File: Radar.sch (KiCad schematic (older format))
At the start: 9 parts

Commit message: fixed library
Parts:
- U? (x3): symbol own:PA -> Radar-rescue:PA-own
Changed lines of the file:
@@
 	7350 3400 7200 3400
 $Comp
-L own:PA U?
+L Radar-rescue:PA-own U?
 U 1 1 5F894269
 P 7800 5200
@@
 $EndComp
 $Comp
-L own:PA U?
+L Radar-rescue:PA-own U?
 U 1 1 5F895397
 P 6700 5200
@@
 $EndComp
 $Comp
-L own:PA U?
+L Radar-rescue:PA-own U?
 U 1 1 5F8A3F2E
 P 5650 5200

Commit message: Architecture of IF
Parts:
- removed U?: PA, symbol Radar-rescue:PA-own
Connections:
- wire segments 8 -> 7
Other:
- moved on the sheet: J?
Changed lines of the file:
@@
 F4 "VCO_TUNE_IN" I L 4950 2500 50
 $EndSheet
-$Sheet
-S 2300 2000 2200 3600
-U 5F88615A
-F0 "Digital" 50
-F1 "digital.sch" 50
-F2 "IF_IN_P" I R 4500 5100 50
-F3 "VCO_TUNE_OUT" O R 4500 2500 50
-F4 "IF_IN_N" I R 4500 5300 50
-$EndSheet
 Wire Wire Line
-	4950 5100 4500 5100
+	4950 5200 4500 5200
 Wire Wire Line
 	4500 2500 4950 2500
 Wire Wire Line
-	8650 2500 7700 2500
+	8200 2500 7700 2500
 Wire Notes Line style solid rgb(132, 0, 0)
 	5500 2500 5650 2500
@@
 L Radar-rescue:PA-own U?
 U 1 1 5F894269
-P 7800 5200
-F 0 "U?" H 7800 5550 50  0001 C CNN
-F 1 "LNA" H 7800 5200 50  0000 R CNN
-F 2 "" H 7800 5200 50  0001 C CNN
-F 3 "" H 7800 5200 50  0001 C CNN
-	1    7800 5200
+P 7400 5200
+F 0 "U?" H 7400 5550 50  0001 C CNN
+F 1 "LNA" H 7400 5200 50  0000 R CNN
+F 2 "" H 7400 5200 50  0001 C CNN
+F 3 "" H 7400 5200 50  0001 C CNN
+	1    7400 5200
 	-1   0    0    1
 $EndComp
@@
 L Radar-rescue:PA-own U?
 U 1 1 5F895397
-P 6700 5200
-F 0 "U?" H 6700 5550 50  0001 C CNN
-F 1 "PA" H 6750 5450 50  0001 R CNN
-F 2 "" H 6700 5200 50  0001 C CNN
-F 3 "" H 6700 5200 50  0001 C CNN
-	1    6700 5200
+P 6300 5200
+F 0 "U?" H 6300 5550 50  0001 C CNN
+F 1 "PA" H 6350 5450 50  0001 R CNN
+F 2 "" H 6300 5200 50  0001 C CNN
+F 3 "" H 6300 5200 50  0001 C CNN
+	1    6300 5200
 	-1   0    0    1
 $EndComp
 Wire Notes Line style solid rgb(132, 0, 0)
-	7250 4200 8050 4200
+	6850 4200 7650 4200
 Wire Notes Line style solid rgb(132, 0, 0)
-	7050 5200 6900 5200
+	6650 5200 6500 5200
 Wire Notes Line style solid rgb(132, 0, 0)
-	8000 5200 8050 5200
+	7600 5200 7650 5200
 Wire Notes Line style solid rgb(132, 0, 0)
-	7250 4200 7250 5000
+	6850 4200 6850 5000
 Wire Notes Line style solid rgb(132, 0, 0)
-	7600 5200 7450 5200
+	7200 5200 7050 5200
 $Sheet
-S 4950 4000 3400 1600
+S 4950 4000 3000 1600
 U 5F88609A
 F0 "Receiver" 50
 F1 "receiver.sch" 50
-F2 "LO_IN" I R 8350 4200 50
-F3 "RF_IN" I R 8350 5200 50
-F4 "IF_OUT_P" O L 4950 5100 50
-F5 "IF_OUT_N" O L 4950 5300 50
+F2 "LO_IN" I R 7950 4200 50
+F3 "RF_IN" I R 7950 5200 50
+F4 "IF_OUT" O L 4950 5200 50
 $EndSheet
 $Comp
 L own:mixer_diagram U?
 U 1 1 5F890667
-P 7250 5200
-F 0 "U?" H 7250 4850 50  0001 C CNN
-F 1 "mixer_diagram" H 7250 5500 50  0001 C CNN
-F 2 "" H 7250 5200 50  0001 C CNN
-F 3 "" H 7250 5200 50  0001 C CNN
-	1    7250 5200
+P 6850 5200
+F 0 "U?" H 6850 4850 50  0001 C CNN
+F 1 "mixer_diagram" H 6850 5500 50  0001 C CNN
+F 2 "" H 6850 5200 50  0001 C CNN
+F 3 "" H 6850 5200 50  0001 C CNN
+	1    6850 5200
 	1    0    0    -1
 $EndComp
@@
 L own:lowpass_diagram U?
 U 1 1 5F89837D
-P 6200 5200
-F 0 "U?" H 6200 5450 50  0001 C CNN
-F 1 "lowpass_diagram" H 6200 4950 50  0001 C CNN
-F 2 "" H 6200 5200 50  0001 C CNN
-F 3 "" H 6200 5200 50  0001 C CNN
-	1    6200 5200
+P 5800 5200
+F 0 "U?" H 5800 5450 50  0001 C CNN
+F 1 "lowpass_diagram" H 5800 4950 50  0001 C CNN
+F 2 "" H 5800 5200 50  0001 C CNN
+F 3 "" H 5800 5200 50  0001 C CNN
+	1    5800 5200
 	1    0    0    -1
 $EndComp
@@
 	6550 2500 7350 2500
 Wire Notes Line style solid rgb(132, 0, 0)
-	6500 5200 6400 5200
-Wire Notes Line style solid rgb(132, 0, 0)
-	6000 5200 5850 5200
+	6100 5200 6000 5200
 $Comp
 L Connector:Conn_Coaxial J?
 U 1 1 5F89AF4D
-P 8850 2500
-F 0 "J?" H 8950 2475 50  0000 L CNN
-F 1 "Transmit Antenna" H 8450 2650 50  0000 L CNN
-F 2 "" H 8850 2500 50  0001 C CNN
-F 3 " ~" H 8850 2500 50  0001 C CNN
-	1    8850 2500
+P 8400 2500
+F 0 "J?" H 8500 2475 50  0000 L CNN
+F 1 "Transmit Antenna" H 8000 2650 50  0000 L CNN
+F 2 "" H 8400 2500 50  0001 C CNN
+F 3 " ~" H 8400 2500 50  0001 C CNN
+	1    8400 2500
 	1    0    0    -1
 $EndComp
@@
 L Connector:Conn_Coaxial J?
 U 1 1 5F89BD12
-P 8800 5200
-F 0 "J?" H 8900 5175 50  0000 L CNN
-F 1 "Receive Antenna" H 8500 5350 50  0000 L CNN
-F 2 "" H 8800 5200 50  0001 C CNN
-F 3 " ~" H 8800 5200 50  0001 C CNN
-	1    8800 5200
+P 8400 5200
+F 0 "J?" H 8500 5175 50  0000 L CNN
+F 1 "Receive Antenna" H 8100 5350 50  0000 L CNN
+F 2 "" H 8400 5200 50  0001 C CNN
+F 3 " ~" H 8400 5200 50  0001 C CNN
+	1    8400 5200
 	1    0    0    -1
 $EndComp
@@
 L power:GND #PWR?
 U 1 1 5F89C296
-P 8850 2700
-F 0 "#PWR?" H 8850 2450 50  0001 C CNN
-F 1 "GND" H 8855 2527 50  0000 C CNN
-F 2 "" H 8850 2700 50  0001 C CNN
-F 3 "" H 8850 2700 50  0001 C CNN
-	1    8850 2700
+P 8400 2700
+F 0 "#PWR?" H 8400 2450 50  0001 C CNN
+F 1 "GND" H 8405 2527 50  0000 C CNN
+F 2 "" H 8400 2700 50  0001 C CNN
+F 3 "" H 8400 2700 50  0001 C CNN
+	1    8400 2700
 	1    0    0    -1
 $EndComp
@@
 L power:GND #PWR?
 U 1 1 5F89C6F1
-P 8800 5400
-F 0 "#PWR?" H 8800 5150 50  0001 C CNN
-F 1 "GND" H 8805 5227 50  0000 C CNN
-F 2 "" H 8800 5400 50  0001 C CNN
-F 3 "" H 8800 5400 50  0001 C CNN
-	1    8800 5400
+P 8400 5400
+F 0 "#PWR?" H 8400 5150 50  0001 C CNN
+F 1 "GND" H 8405 5227 50  0000 C CNN
+F 2 "" H 8400 5400 50  0001 C CNN
+F 3 "" H 8400 5400 50  0001 C CNN
+	1    8400 5400
 	1    0    0    -1
 $EndComp
-$Comp
-L Radar-rescue:PA-own U?
-U 1 1 5F8A3F2E
-P 5650 5200
-F 0 "U?" H 5650 5550 50  0001 C CNN
-F 1 "PA" H 5700 5450 50  0001 R CNN
-F 2 "" H 5650 5200 50  0001 C CNN
-F 3 "" H 5650 5200 50  0001 C CNN
-	1    5650 5200
-	-1   0    0    1
-$EndComp
 Wire Wire Line
-	8350 5200 8600 5200
+	7950 5200 8200 5200
 Wire Wire Line
-	4950 5300 4500 5300
+	8100 3400 8100 4200
 Wire Wire Line
-	8500 3400 8500 4200
+	8100 4200 7950 4200
 Wire Wire Line
-	8500 4200 8350 4200
-Wire Wire Line
-	7700 3400 8500 3400
-Wire Notes Line style solid rgb(132, 0, 0)
-	5650 5100 5350 5100
-Wire Notes Line style solid rgb(132, 0, 0)
-	5650 5300 5350 5300
+	7700 3400 8100 3400
 Wire Notes Line
 	4800 1800 4800 5850
@@
 Text Notes 4550 1950 2    100  ~ 0
 Digital Board
+$Sheet
+S 2300 2000 2200 3600
+U 5F88615A
+F0 "Digital" 50
+F1 "digital.sch" 50
+F2 "IF_IN" I R 4500 5200 50
+F3 "VCO_TUNE_OUT" O R 4500 2500 50
+$EndSheet
+Wire Notes Line style solid rgb(132, 0, 0)
+	5350 5200 5600 5200
 $EndSCHEMATC

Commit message: Finished IF
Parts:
- removed J?: Receive Antenna, symbol Connector:Conn_Coaxial
- removed U?: mixer_diagram, symbol own:mixer_diagram
- removed U?: LNA, symbol Radar-rescue:PA-own
- removed U?: PA, symbol Radar-rescue:PA-own
- removed U?: lowpass_diagram, symbol own:lowpass_diagram
- added J1: Receive_Antenna, symbol Connector:Conn_Coaxial
- added J2: VCO_Tune, symbol Connector:Conn_Coaxial
- added J4: Output, symbol Connector:Conn_Coaxial
- added U1: LNA_1, symbol own:amplifier_diagram
- added U2: SW1, symbol own:switch
- added U3: LNA_2, symbol own:amplifier_diagram
- added U5: SW2, symbol own:switch
- added U7: mixer_diagram, symbol own:mixer_diagram
- added U8: PGA, symbol own:amplifier_diagram
- added U9: lowpass_diagram, symbol own:lowpass_diagram
- gave numbers to parts that had none: 3
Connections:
- net labels added: IF_IN, IF_OUT, LO_IN, LO_OUT, PA_ON, PGA_CTRL, RF_IN, SW_CONTROL
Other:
- note removed: "Digital Board"
- note removed: "RF Board\n"
- moved on the sheet: J3

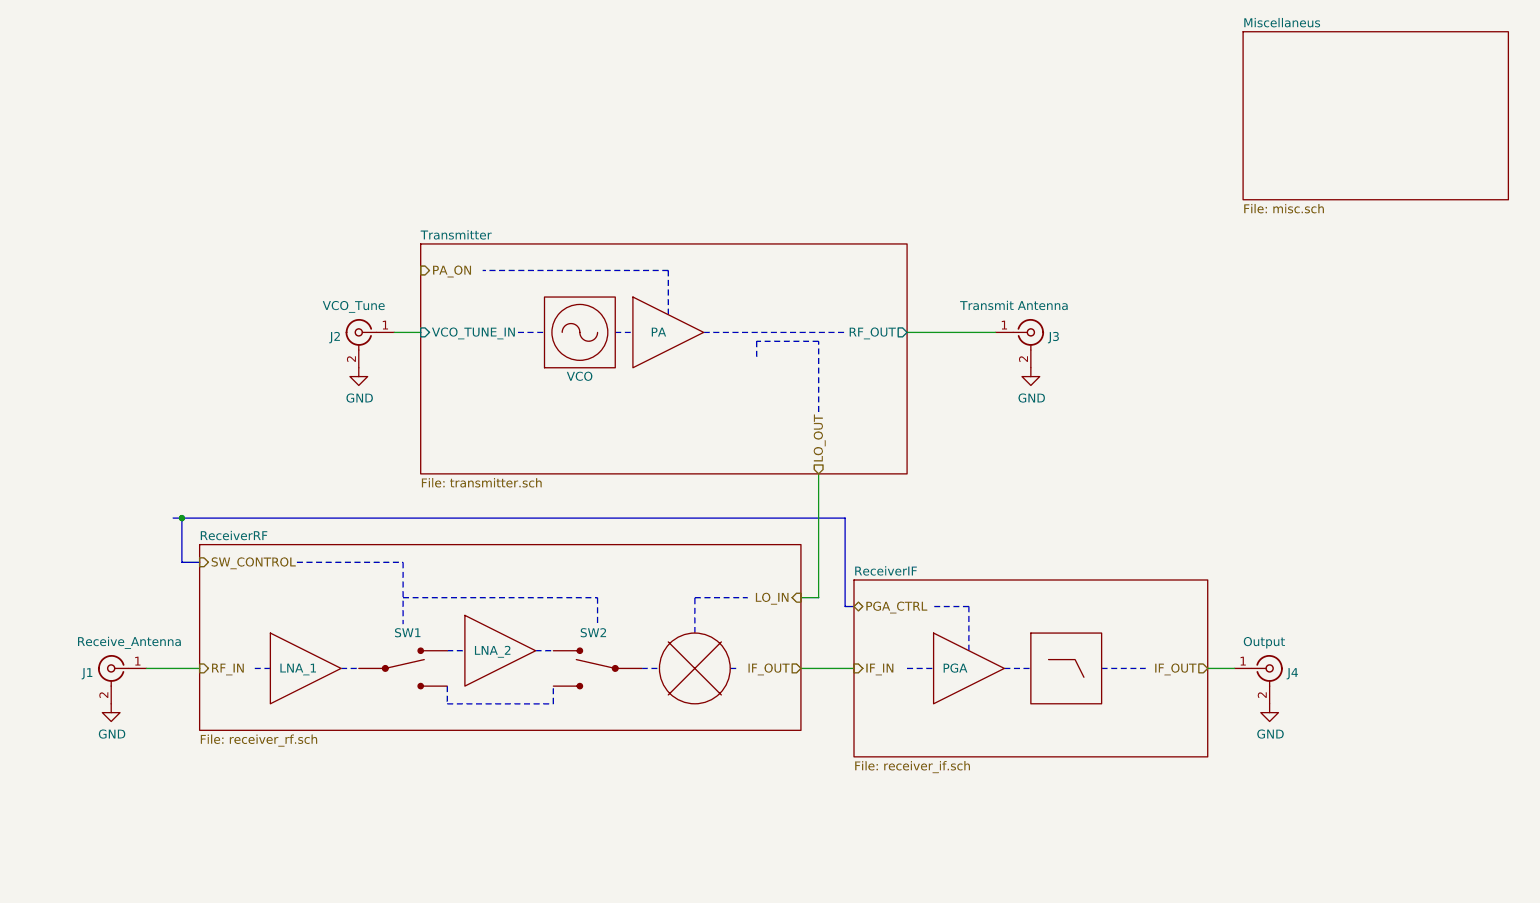
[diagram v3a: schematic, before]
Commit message: Fixed sheets and changed footprints and capacitor values
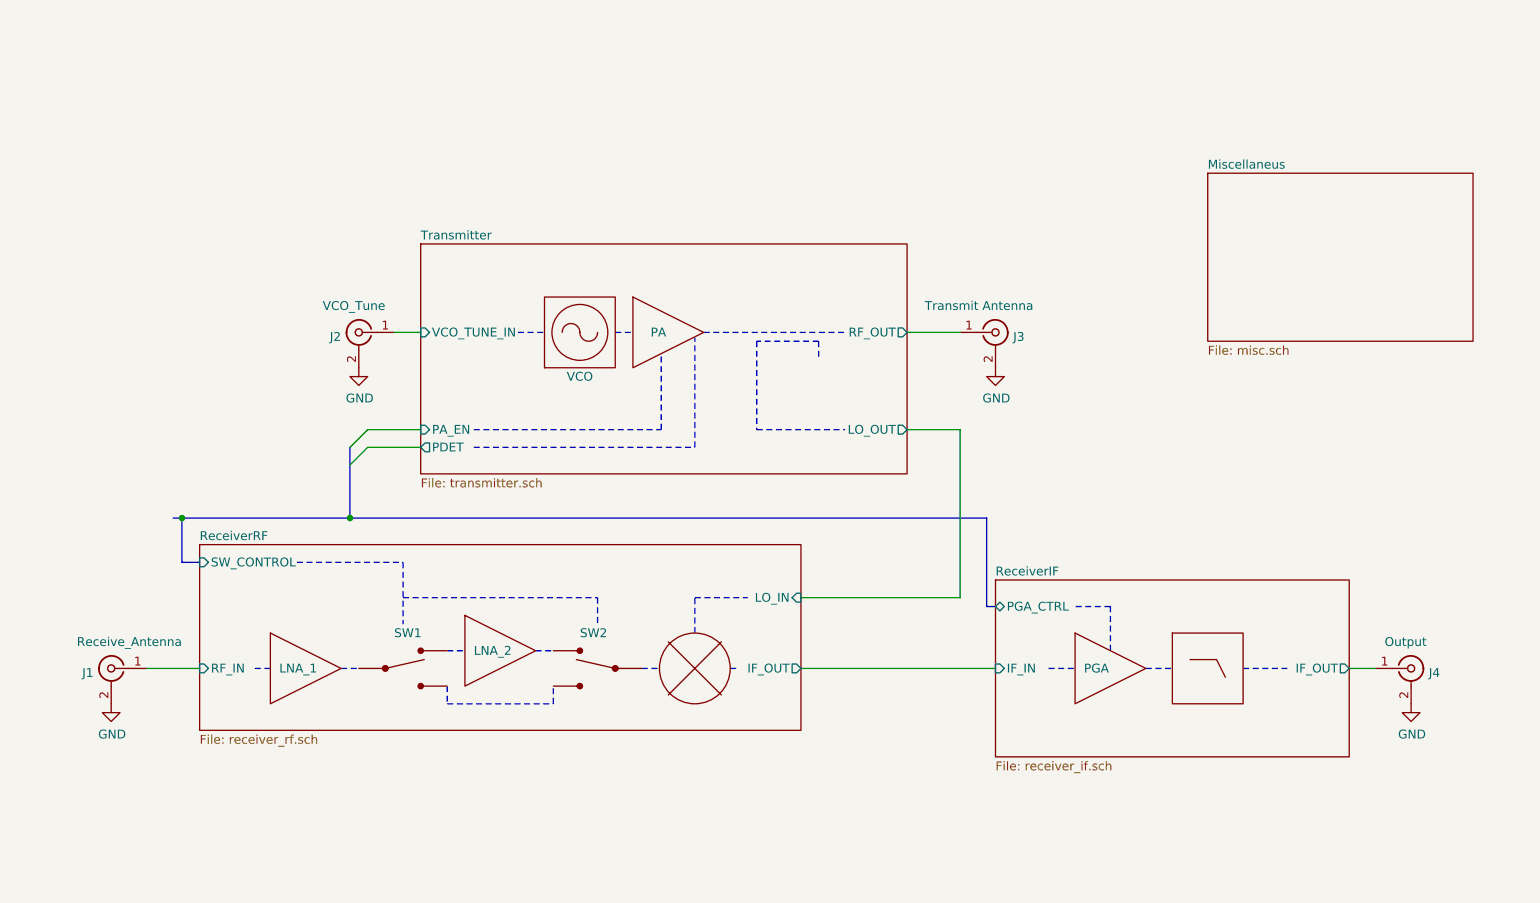
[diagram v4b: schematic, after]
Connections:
- net IF_IN renamed ReceiverIF/IF_OUT
- net RF_IN renamed ReceiverRF/RF_IN
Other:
- moved on the sheet: J3, J4
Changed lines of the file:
@@
 Comment4 ""
 $EndDescr
-$Sheet
-S 3900 2200 2750 1300
-U 5F886026
-F0 "Transmitter" 50
-F1 "transmitter.sch" 50
-F2 "RF_OUT" O R 6650 2700 50
-F3 "VCO_TUNE_IN" I L 3900 2700 50
-$EndSheet
-Wire Wire Line
-	7150 2700 6650 2700
 Wire Notes Line style solid rgb(132, 0, 0)
 	4450 2700 4600 2700
@@
 	5000 2700 5100 2700
 Wire Notes Line style solid rgb(132, 0, 0)
-	5800 2750 5800 2850
-Wire Notes Line style solid rgb(132, 0, 0)
 	6150 2750 5800 2750
-Wire Notes Line style solid rgb(132, 0, 0)
-	6150 3150 6150 2750
 $Comp
 L own:vco_diagram U4
@@
 L Connector:Conn_Coaxial J3
 U 1 1 5F89AF4D
-P 7350 2700
-F 0 "J3" H 7450 2675 50  0000 L CNN
-F 1 "Transmit Antenna" H 6950 2850 50  0000 L CNN
-F 2 "" H 7350 2700 50  0001 C CNN
-F 3 " ~" H 7350 2700 50  0001 C CNN
-	1    7350 2700
+P 7150 2700
+F 0 "J3" H 7250 2675 50  0000 L CNN
+F 1 "Transmit Antenna" H 6750 2850 50  0000 L CNN
+F 2 "" H 7150 2700 50  0001 C CNN
+F 3 " ~" H 7150 2700 50  0001 C CNN
+	1    7150 2700
 	1    0    0    -1
 $EndComp
@@
 L power:GND #PWR0101
 U 1 1 5F89C296
-P 7350 2900
-F 0 "#PWR0101" H 7350 2650 50  0001 C CNN
-F 1 "GND" H 7355 2727 50  0000 C CNN
-F 2 "" H 7350 2900 50  0001 C CNN
-F 3 "" H 7350 2900 50  0001 C CNN
-	1    7350 2900
+P 7150 2900
+F 0 "#PWR0101" H 7150 2650 50  0001 C CNN
+F 1 "GND" H 7155 2727 50  0000 C CNN
+F 2 "" H 7150 2900 50  0001 C CNN
+F 3 "" H 7150 2900 50  0001 C CNN
+	1    7150 2900
 	1    0    0    -1
 $EndComp
 $Sheet
-S 6350 4100 2000 1000
+S 7150 4100 2000 1000
 U 605249CC
 F0 "ReceiverIF" 50
 F1 "receiver_if.sch" 50
+F2 "IF_IN" I L 7150 4600 50
+F3 "IF_OUT" O R 9150 4600 50
+F4 "PGA_CTRL" B L 7150 4250 50
 $EndSheet
 $Sheet
@@
 F0 "ReceiverRF" 50
 F1 "receiver_rf.sch" 50
+F2 "RF_IN" I L 2650 4600 50
+F3 "LO_IN" I R 6050 4200 50
+F4 "IF_OUT" O R 6050 4600 50
+F5 "SW_CONTROL" I L 2650 4000 50
 $EndSheet
 $Comp
@@
 Wire Notes Line style solid rgb(132, 0, 0)
 	5150 4600 5250 4600
-Text HLabel 2650 4600 2    50   Output ~ 0
-RF_IN
 Wire Notes Line style solid rgb(132, 0, 0)
 	3050 4600 2950 4600
-Text HLabel 6050 4600 0    50   Input ~ 0
-IF_OUT
-Text HLabel 6050 4200 0    50   Output ~ 0
-LO_IN
-Text HLabel 6150 3500 1    50   Input ~ 0
-LO_OUT
 Wire Notes Line style solid rgb(132, 0, 0)
 	5450 4400 5450 4200
@@
 Wire Notes Line style solid rgb(132, 0, 0)
 	5450 4200 5750 4200
-Wire Wire Line
-	6050 4200 6150 4200
-Wire Wire Line
-	6150 4200 6150 3500
 $Comp
 L power:GND #PWR0102
@@
 Wire Notes Line rgb(132, 0, 0)
 	4900 4200 4900 4350
-Text HLabel 2650 4000 2    50   Output ~ 0
-SW_CONTROL
 Wire Notes Line rgb(132, 0, 0)
 	3200 4000 3800 4000
-Text HLabel 6350 4600 2    50   Output ~ 0
-IF_IN
 $Comp
 L own:amplifier_diagram U8
 U 1 1 6053C1B4
-P 7000 4600
-F 0 "U8" H 7000 4950 50  0001 C CNN
-F 1 "PGA" H 6850 4600 50  0000 L CNN
-F 2 "" H 7000 4600 50  0001 C CNN
-F 3 "" H 7000 4600 50  0001 C CNN
-	1    7000 4600
+P 7800 4600
+F 0 "U8" H 7800 4950 50  0001 C CNN
+F 1 "PGA" H 7650 4600 50  0000 L CNN
+F 2 "" H 7800 4600 50  0001 C CNN
+F 3 "" H 7800 4600 50  0001 C CNN
+	1    7800 4600
 	1    0    0    -1
 $EndComp
@@
 L own:lowpass_diagram U9
 U 1 1 6053C876
-P 7550 4600
-F 0 "U9" H 7550 4850 50  0001 C CNN
-F 1 "lowpass_diagram" H 7550 4350 50  0001 C CNN
-F 2 "" H 7550 4600 50  0001 C CNN
-F 3 "" H 7550 4600 50  0001 C CNN
-	1    7550 4600
-	1    0    0    -1
-$EndComp
-Wire Notes Line style solid rgb(132, 0, 0)
-	6650 4600 6800 4600
+P 8350 4600
+F 0 "U9" H 8350 4850 50  0001 C CNN
+F 1 "lowpass_diagram" H 8350 4350 50  0001 C CNN
+F 2 "" H 8350 4600 50  0001 C CNN
+F 3 "" H 8350 4600 50  0001 C CNN
+	1    8350 4600
+	1    0    0    -1
+$EndComp
+Wire Notes Line style solid rgb(132, 0, 0)
+	7450 4600 7600 4600
 Wire Notes Line rgb(132, 0, 0)
 	3800 4000 3800 4350
 Wire Notes Line style solid rgb(132, 0, 0)
-	7200 4600 7350 4600
-Wire Notes Line style solid rgb(132, 0, 0)
-	7750 4600 8000 4600
-Text HLabel 8350 4600 0    50   Input ~ 0
-IF_OUT
-Wire Wire Line
-	6350 4600 6050 4600
+	8000 4600 8150 4600
+Wire Notes Line style solid rgb(132, 0, 0)
+	8550 4600 8800 4600
 $Comp
 L Connector:Conn_Coaxial J4
 U 1 1 6053E780
-P 8700 4600
-F 0 "J4" H 8800 4575 50  0000 L CNN
-F 1 "Output" H 8550 4750 50  0000 L CNN
-F 2 "" H 8700 4600 50  0001 C CNN
-F 3 " ~" H 8700 4600 50  0001 C CNN
-	1    8700 4600
+P 9500 4600
+F 0 "J4" H 9600 4575 50  0000 L CNN
+F 1 "Output" H 9350 4750 50  0000 L CNN
+F 2 "" H 9500 4600 50  0001 C CNN
+F 3 " ~" H 9500 4600 50  0001 C CNN
+	1    9500 4600
 	1    0    0    -1
 $EndComp
@@
 L power:GND #PWR0103
 U 1 1 6053F51D
-P 8700 4800
-F 0 "#PWR0103" H 8700 4550 50  0001 C CNN
-F 1 "GND" H 8705 4627 50  0000 C CNN
-F 2 "" H 8700 4800 50  0001 C CNN
-F 3 "" H 8700 4800 50  0001 C CNN
-	1    8700 4800
-	1    0    0    -1
-$EndComp
-Wire Wire Line
-	8500 4600 8350 4600
-Wire Notes Line rgb(132, 0, 0)
-	5300 2600 5300 2350
-Wire Notes Line rgb(132, 0, 0)
-	5300 2350 4250 2350
-Text HLabel 3900 2350 2    50   Output ~ 0
-PA_ON
-Wire Notes Line rgb(132, 0, 0)
-	7000 4500 7000 4250
-Wire Notes Line rgb(132, 0, 0)
-	7000 4250 6800 4250
-Text HLabel 6350 4250 2    50   BiDi ~ 0
-PGA_CTRL
+P 9500 4800
+F 0 "#PWR0103" H 9500 4550 50  0001 C CNN
+F 1 "GND" H 9505 4627 50  0000 C CNN
+F 2 "" H 9500 4800 50  0001 C CNN
+F 3 "" H 9500 4800 50  0001 C CNN
+	1    9500 4800
+	1    0    0    -1
+$EndComp
+Wire Wire Line
+	9300 4600 9150 4600
+Wire Notes Line rgb(132, 0, 0)
+	7800 4500 7800 4250
+Wire Notes Line rgb(132, 0, 0)
+	7800 4250 7600 4250
 $Comp
 L Connector:Conn_Coaxial J2
@@
 	3750 2700 3900 2700
 Wire Bus Line
-	6350 4250 6300 4250
-Wire Bus Line
-	6300 4250 6300 3750
-Wire Bus Line
-	6300 3750 2550 3750
+	7150 4250 7100 4250
+Wire Bus Line
+	7100 4250 7100 3750
 Wire Bus Line
 	2650 4000 2550 4000
@@
 	2550 4000 2550 3750
 $Sheet
-S 8550 1000 1500 950
+S 8350 1800 1500 950
 U 60869BAE
 F0 "Miscellaneus" 50
 F1 "misc.sch" 50
 $EndSheet
+$Sheet
+S 3900 2200 2750 1300
+U 5F886026
+F0 "Transmitter" 50
+F1 "transmitter.sch" 50
+F2 "RF_OUT" O R 6650 2700 50
+F3 "LO_OUT" O R 6650 3250 50
+F4 "PDET" O L 3900 3350 50
+F5 "PA_EN" I L 3900 3250 50
+F6 "VCO_TUNE_IN" I L 3900 2700 50
+$EndSheet
+Wire Notes Line rgb(132, 0, 0)
+	4200 3250 5260 3250
+Wire Notes Line rgb(132, 0, 0)
+	5260 3250 5260 2820
+Wire Notes Line rgb(132, 0, 0)
+	4200 3350 5450 3350
+Wire Notes Line rgb(132, 0, 0)
+	5450 3350 5450 2730
+Entry Wire Line
+	3600 3350 3500 3450
+Entry Wire Line
+	3600 3250 3500 3350
+Wire Wire Line
+	3600 3250 3900 3250
+Wire Wire Line
+	3600 3350 3900 3350
+Wire Bus Line
+	2550 3750 3500 3750
+Wire Notes Line style solid rgb(132, 0, 0)
+	6150 2750 6150 2850
+Wire Notes Line style solid rgb(132, 0, 0)
+	5800 3250 6300 3250
+Wire Notes Line style solid rgb(132, 0, 0)
+	5800 2750 5800 3250
+Wire Wire Line
+	6050 4600 7150 4600
+Wire Wire Line
+	6950 4200 6950 3250
+Wire Wire Line
+	6950 3250 6650 3250
+Wire Wire Line
+	6050 4200 6950 4200
+Wire Bus Line
+	3500 3750 7100 3750
+Connection ~ 3500 3750
+Wire Wire Line
+	6950 2700 6650 2700
+Wire Bus Line
+	3500 3350 3500 3750
 $EndSCHEMATC

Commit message: Schematic finishing touches
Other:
- moved on the sheet: J1, J2, J3, J4

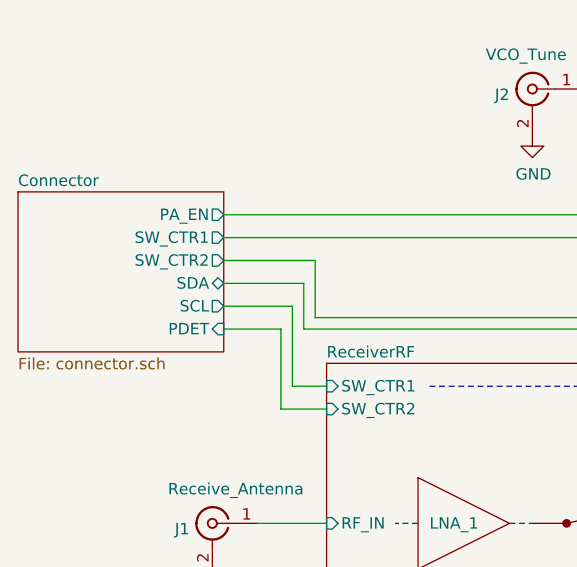
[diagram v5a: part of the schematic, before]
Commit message: Added connector
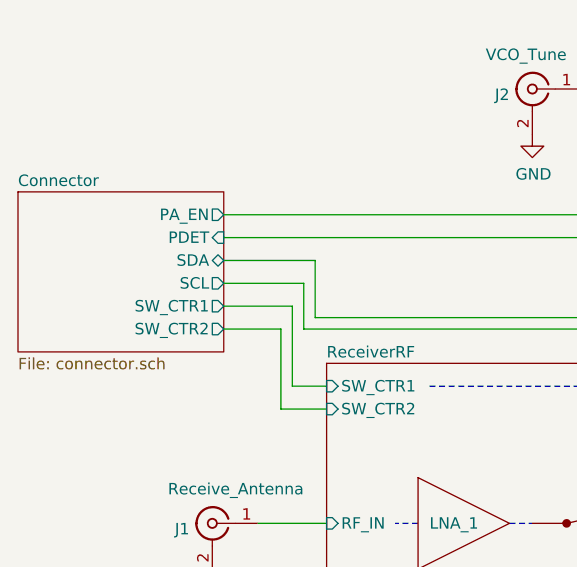
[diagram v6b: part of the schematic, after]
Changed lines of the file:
@@
 Wire Wire Line
 	7400 4500 7400 3950
-Wire Wire Line
-	2500 3500 4200 3500
-Wire Wire Line
-	2500 3600 4200 3600
 $Sheet
 S 1600 3400 900  700
@@
 F1 "connector.sch" 50
 F2 "PA_EN" O R 2500 3500 50
-F3 "SW_CTR1" O R 2500 3600 50
-F4 "SW_CTR2" O R 2500 3700 50
-F5 "SDA" B R 2500 3800 50
-F6 "SCL" O R 2500 3900 50
-F7 "PDET" I R 2500 4000 50
+F3 "SW_CTR1" O R 2500 3900 50
+F4 "SW_CTR2" O R 2500 4000 50
+F5 "SDA" B R 2500 3700 50
+F6 "SCL" O R 2500 3800 50
+F7 "PDET" I R 2500 3600 50
 $EndSheet
 Wire Wire Line
@@
 Wire Wire Line
 	2900 3950 7400 3950
+Wire Wire Line
+	2500 3600 4200 3600
+Wire Wire Line
+	2500 3500 4200 3500
 $EndSCHEMATC
